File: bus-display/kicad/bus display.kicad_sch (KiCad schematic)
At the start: 40 parts, among them U1 74LS00, U10 INND-TS40, U11 INND-TS40, U2 INND-TS40, U3 NE555P, U4 SST39SF010, U5 INND-TS40, U6 SST39SF010, U7 INND-TS40, U8 INND-TS40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

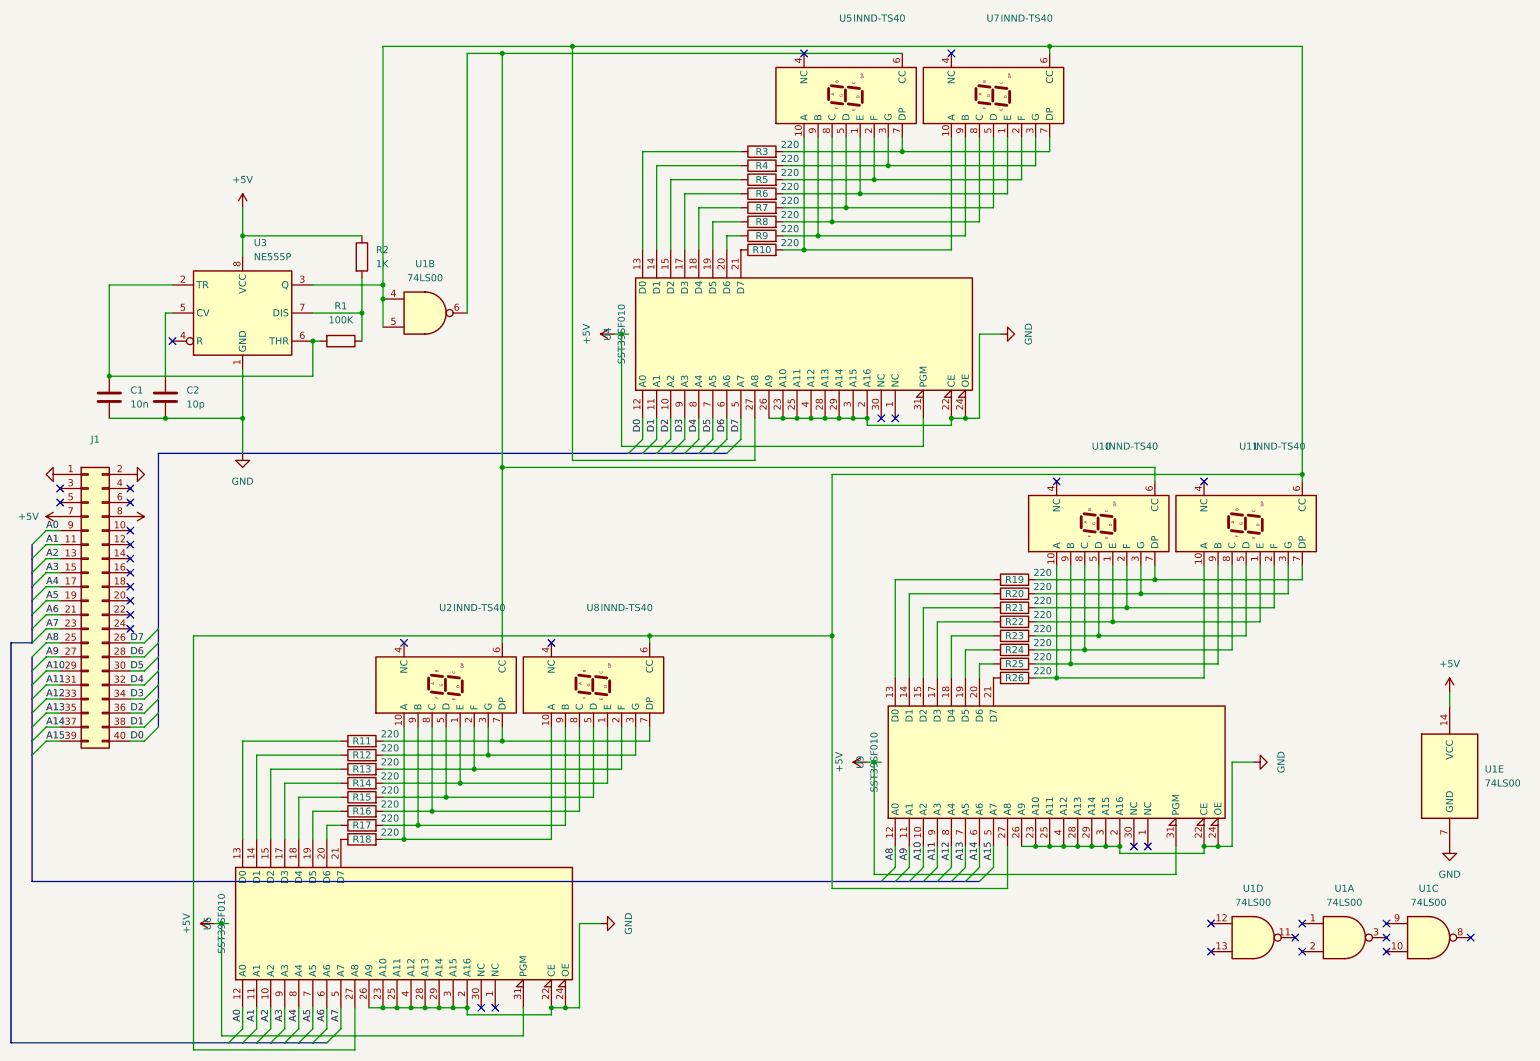
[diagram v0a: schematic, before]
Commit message: finished bus display
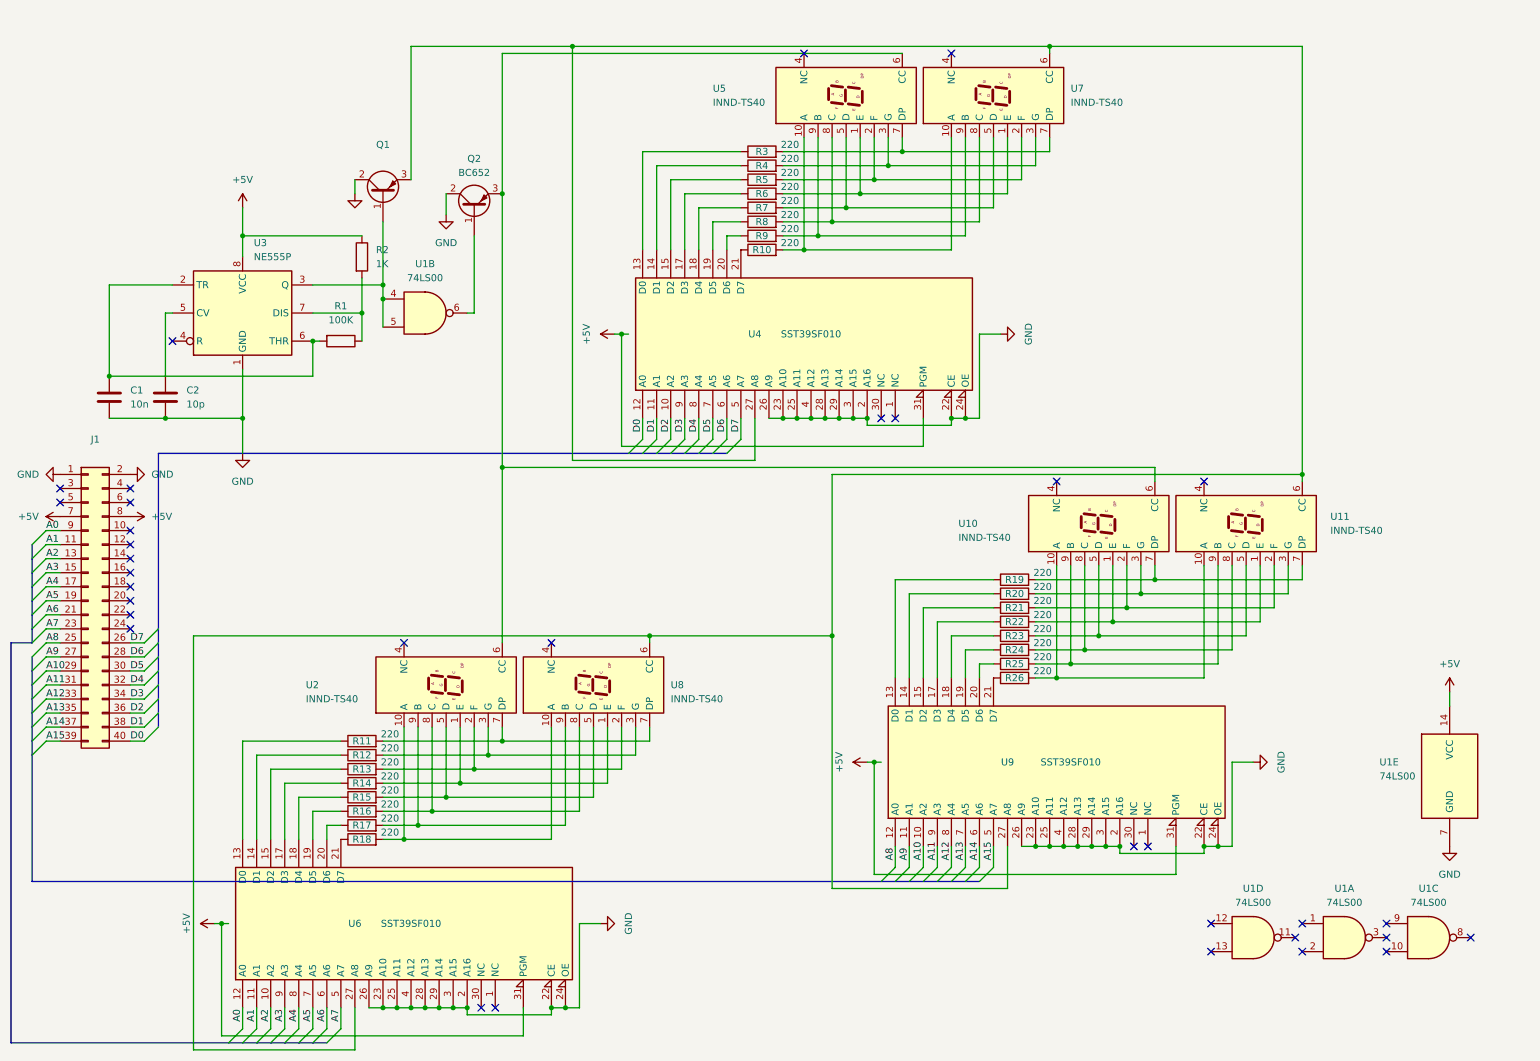
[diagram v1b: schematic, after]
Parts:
- added Q1: (no value), symbol Device:Q_PNP_BCE
- added Q2: BC652, symbol Device:Q_PNP_BCE
- J1: footprint (none) -> Connector_PinHeader_2.54mm:PinHeader_2x20_P2.54mm_Vertical
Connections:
- net GND: now also Q1.2 (C), Q2.2 (C)
- net at U11.6 (CC), U4.27 (A8), U6.27 (A8)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: now also Q1.3 (E); no longer U1.4, U1.5, U3.3 (Q)
- net at U10.6 (CC), U2.6 (CC), U5.6 (CC): now also Q2.3 (E); no longer U1.6
- new net: Q1.1 (B), U1.4, U1.5, U3.3 (Q)
- new net: Q2.1 (B), U1.6
